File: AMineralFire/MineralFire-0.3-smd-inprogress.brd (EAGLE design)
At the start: 95.9 x 68.1 mm, 91 parts, among them IC3 LM358D, Q1 20MHz, Q2 20MHz, Q3 MMBT3906LT1SMD, Q4 MMBT3906LT1SMD, Q5 MMBT3906LT1SMD, Q6 MMBT3906LT1SMD, Q7 MMBT3906LT1SMD, Q8 MMBT3906LT1SMD, Q9 MMBT3906LT1SMD, T1 200mA/40V, T2 200mA/40V, T3 200mA/40V, T4 200mA/40V, T5 200mA/40V, U1 ATMEGA328P_TQFP, U2 7805, U4 ATMEGA328P_TQFP, U5 7805

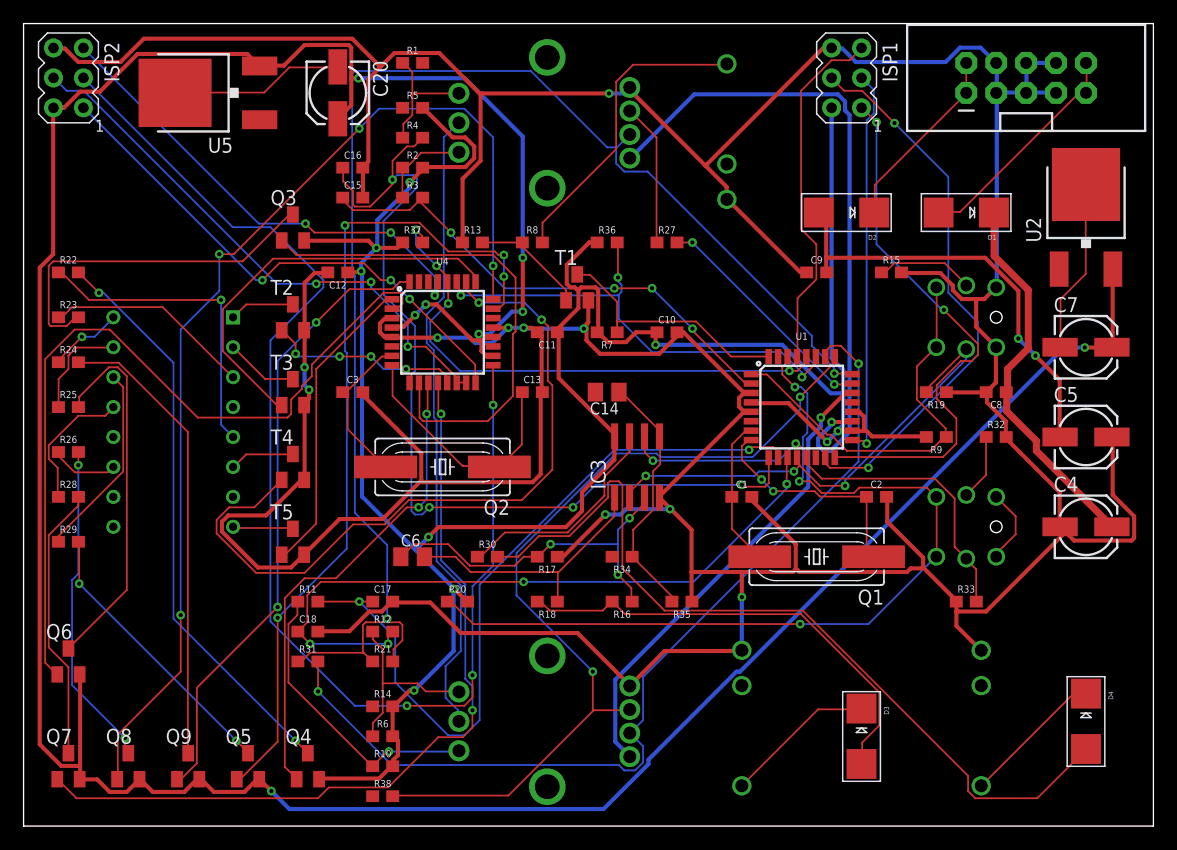
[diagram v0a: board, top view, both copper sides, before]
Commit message: Fixed routing errors
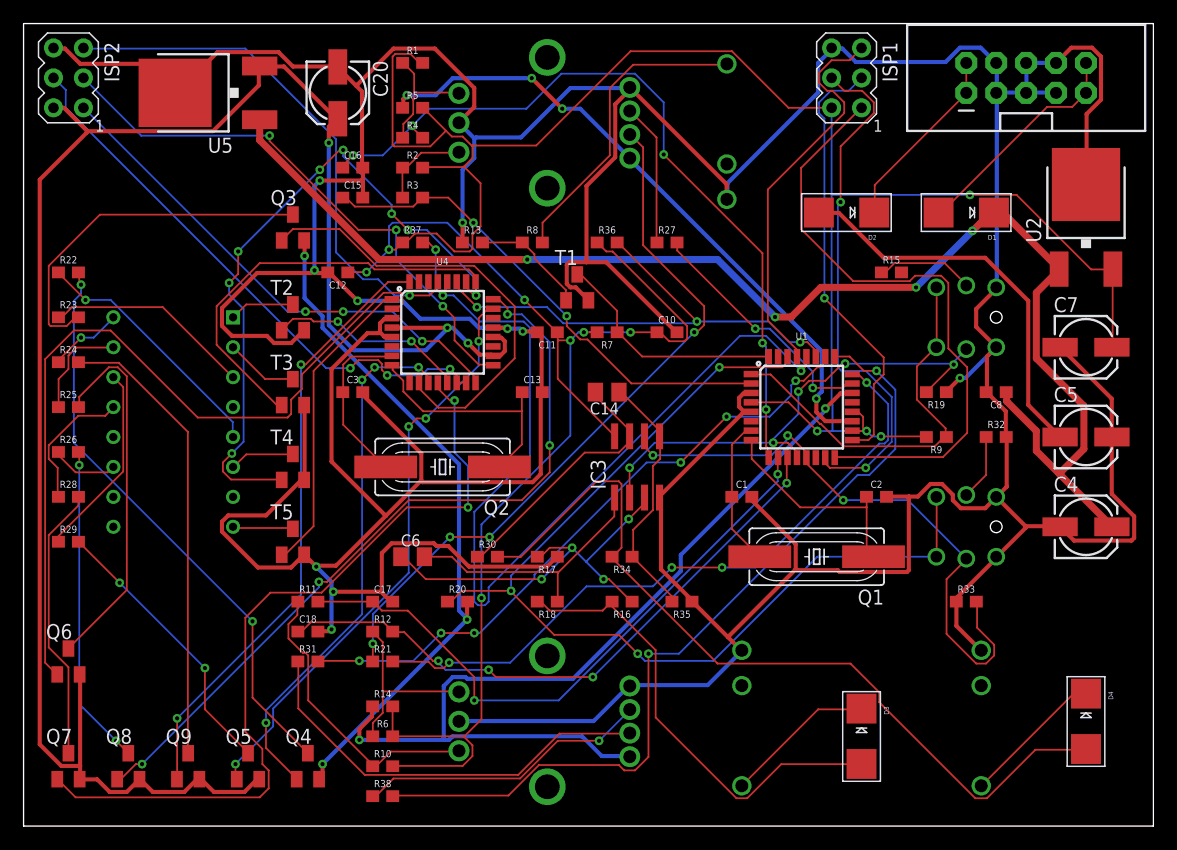
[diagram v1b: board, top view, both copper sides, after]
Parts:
- removed C9: 0.1uF, SparkFun-Capacitors:0603
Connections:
- removed net +12V: C4.+, C8.1, D1.C
- removed net +12V1: U2.1
- removed net +12V2: U5.1
- removed net -12V: C5.-, C9.2, D2.A
- removed net B_TRIG1: R5.1
- removed net B_TRIG2: R14.1
- removed net CS: U1.14
- removed net GND1: C7.-, U2.4
- removed net GND2: C20.-, U5.4
- removed net N$25: C14.2
- removed net N$26: R34.2
- removed net N$29: BUT1.3, BUT1.4
- removed net N$4: R1.2
- new net 12V: C4.+, C8.1, D1.C, U2.1, U5.1
- new net 5V: C10.1, C11.1, C12.1, C7.+, IC3.8, ISP1.2, R1.2, R10.2, R14.2, R2.2, R36.1, R37.1, R5.2, R6.2, R7.2, R9.2, U1.18, U1.20, U1.4, U2.3
- new net N$36: ENC2.+R, R31.1
- new net N$38: C5.-, D2.A
- net +5V: no longer C10.1, C11.1, C12.1, IC3.8, ISP1.2, R10.2, R14.2, R2.2, R36.1, R37.1, R5.2, R6.2, R7.2, R9.2, U1.18, U1.20, U1.4
- net 5VDISP: no longer C7.+, U2.3
- net BUT1: now also R5.1
- net BUT2: now also R14.1
- net ENC1-R: no longer ENC1.+R, R21.1, R31.1
- net ENC2-G: no longer ENC2.+G
- net ENC2-R: no longer ENC2.+R
- net GND: now also BUT1.3, BUT1.4, C20.-, C7.-, ENC1.C, ENC2.C, U2.4, U5.4; no longer C9.1
- net N$19: now also C14.2
- net N$22: now also R34.2
- net N$3: now also ENC1.+R, R21.1; no longer ENC1.C, ENC2.C
- net N$35: now also ENC2.+G
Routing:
- net 5V: track 0.00 -> 274.3 mm, vias 0 -> 11
- net +5V: track 210.3 -> 58.2 mm, vias 9 -> 3
- net 12V: track 0.00 -> 117.3 mm, vias 0 -> 4
- net 5VDISP: track 266.4 -> 157.1 mm, vias 8 -> 3
- net GND: track 477.5 -> 554.1 mm
- net ENC1-R: track 120.6 -> 57.5 mm, vias 2 -> 4
- net SCK2: track 107.6 -> 47.8 mm
- net BUT2: track 40.1 -> 77.7 mm, vias 1 -> 2
- net -12V: track 36.7 -> 0.00 mm, vias 2 -> 0
- net N$36: track 0.00 -> 36.0 mm
- net SCL: track 46.3 -> 81.3 mm, vias 4 -> 3
- net N$38: track 0.00 -> 33.5 mm
- net +12V: track 32.3 -> 0.00 mm
- net C-SEGF: track 91.3 -> 65.5 mm
- net N$35: track 0.00 -> 24.9 mm, vias 0 -> 1
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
